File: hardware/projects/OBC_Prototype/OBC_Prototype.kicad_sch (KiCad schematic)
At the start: 1 part, among them U1 SAM-M10Q-00B

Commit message: add a bunch of parts to the kicad lib
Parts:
- U1: footprint SAM-M10Q_UBL -> obc:SAM-M10Q_UBL; MPN (none) -> SAM-M10Q-00B; Manufacturer (none) -> u-blox
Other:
- added sheet Power Management (../../shared/power_management.kicad_sch)
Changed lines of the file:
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@@
 			)
 		)
-		(property "Footprint" "SAM-M10Q_UBL"
+		(property "Footprint" "obc:SAM-M10Q_UBL"
 			(at 52.07 43.18 0)
 			(hide yes)
@@
 			)
 		)
-		(property "Datasheet" "SAM-M10Q-00B"
+		(property "Datasheet" "https://content.u-blox.com/sites/default/files/documents/SAM-M10Q_DataSheet_UBX-22013293.pdf"
 			(at 52.07 43.18 0)
 			(hide yes)
@@
 		(property "Description" ""
 			(at 52.07 43.18 0)
+			(hide yes)
+			(show_name no)
+			(do_not_autoplace no)
+			(effects
+				(font
+					(size 1.27 1.27)
+				)
+			)
+		)
+		(property "Manufacturer" "u-blox"
+			(at 76.962 80.01 0)
+			(hide yes)
+			(show_name no)
+			(do_not_autoplace no)
+			(effects
+				(font
+					(size 1.27 1.27)
+				)
+			)
+		)
+		(property "MPN" "SAM-M10Q-00B"
+			(at 90.678 80.01 0)
 			(hide yes)
 			(show_name no)
@@
 				)
 			)
+		)
+	)
+	(sheet
+		(at 158.75 44.45)
+		(size 73.66 52.07)
+		(exclude_from_sim no)
+		(in_bom yes)
+		(on_board yes)
+		(dnp no)
+		(fields_autoplaced yes)
+		(stroke
+			(width 0.1524)
+			(type solid)
+		)
+		(fill
+			(color 0 0 0 0)
+		)
+		(property "Sheetname" "Power Management"
+			(at 158.75 43.7384 0)
+			(show_name no)
+			(do_not_autoplace no)
+			(effects
+				(font
+					(size 1.27 1.27)
+				)
+				(justify left bottom)
+			)
+		)
+		(property "Sheetfile" "../../shared/power_management.kicad_sch"
+			(at 158.75 97.1046 0)
+			(show_name no)
+			(do_not_autoplace no)
+			(effects
+				(font
+					(size 1.27 1.27)
+				)
+				(justify left top)
+			)
+		)
+		(instances
+			(project "OBC_Prototype"
+				(path "/9592e112-fc73-4f3e-a0d8-ab6827836a9f"
+					(page "2")
+				)
+			)

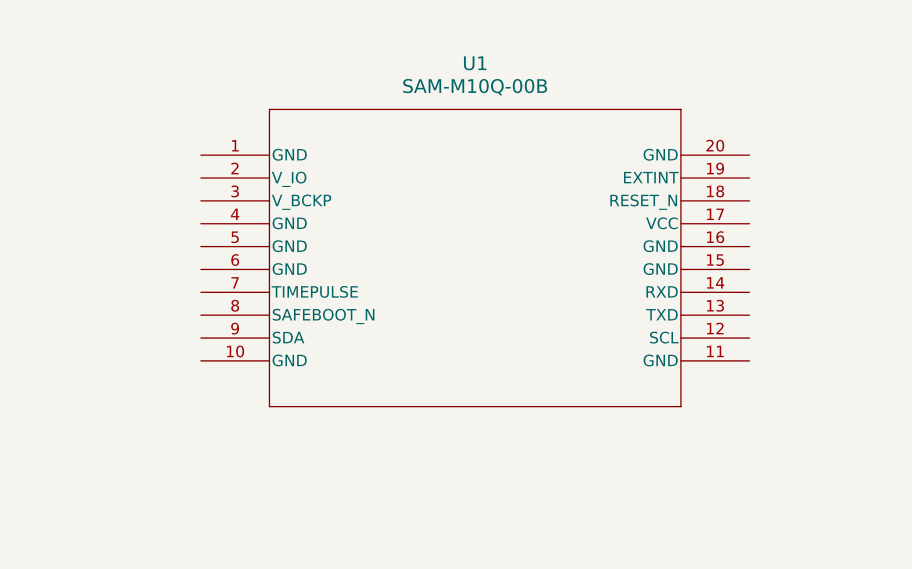
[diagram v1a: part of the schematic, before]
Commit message: Adding most basic components to schematic
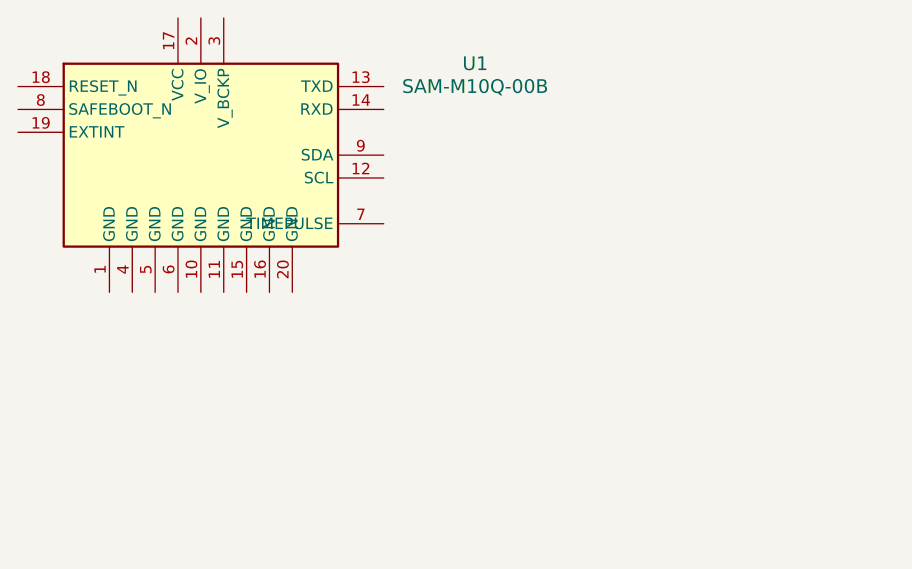
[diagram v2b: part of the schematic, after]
